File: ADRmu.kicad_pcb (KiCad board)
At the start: 4 copper layers, 160 x 100 mm, 67 parts, among them J1 DIN41612_02x16_AC_EvenPins, J10 Conn_01x01, J11 Conn_01x01, J12 Conn_01x01, J2 10Vf, J3 10Vs, J4 ADRf, J5 ADRs, J6 return, J7 guard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

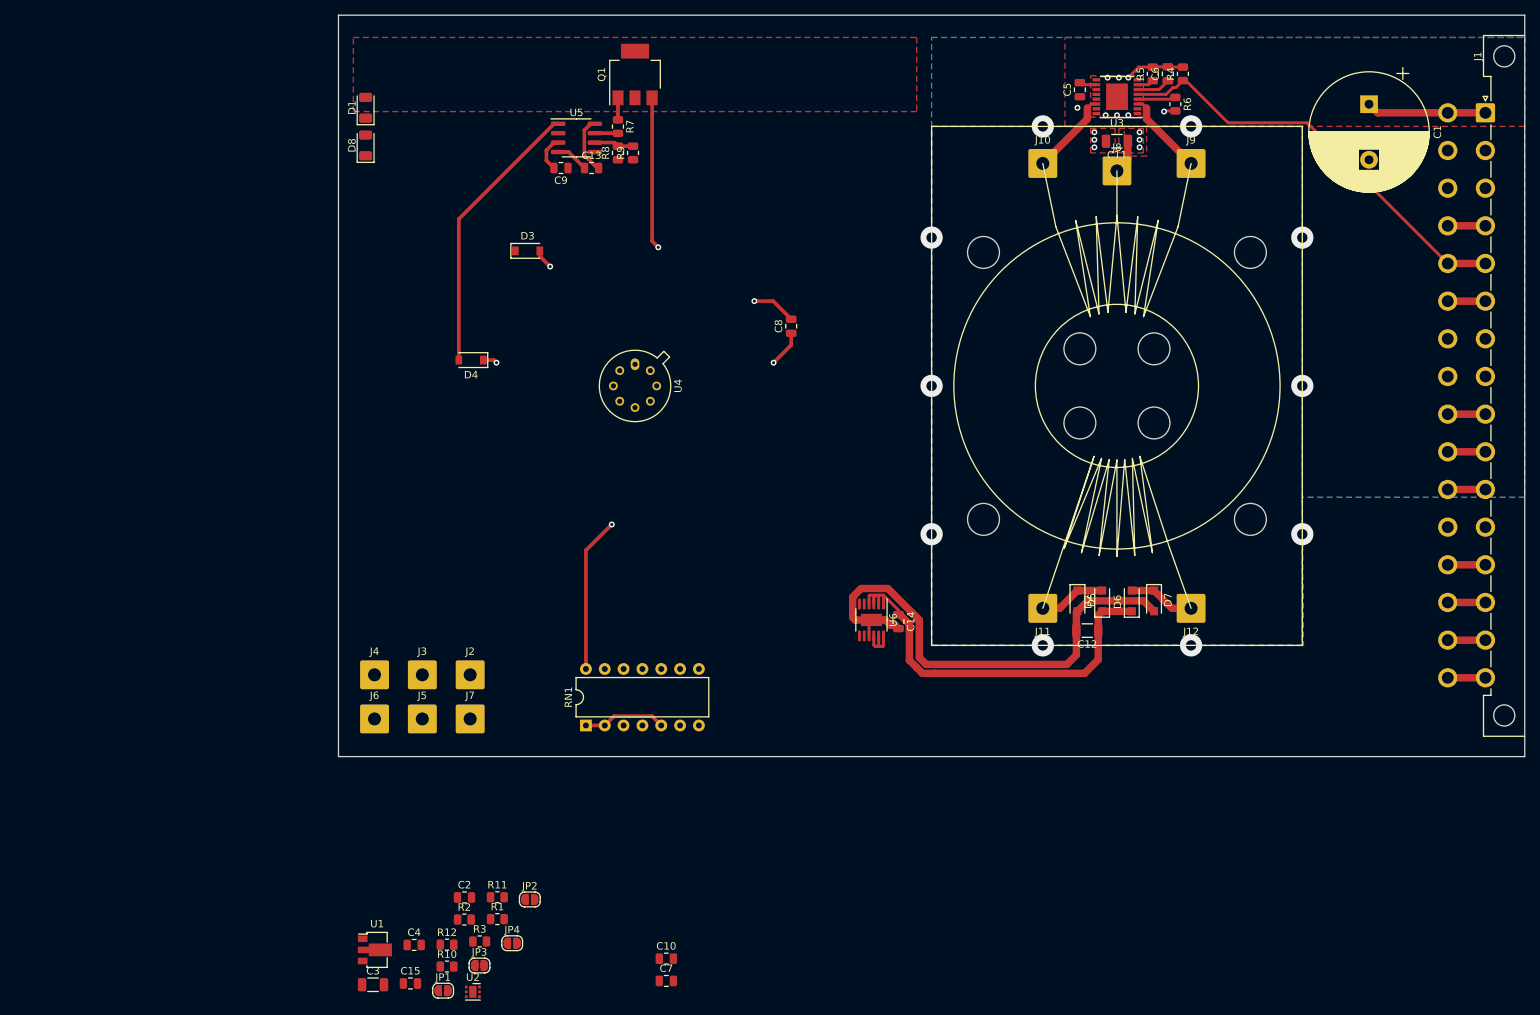
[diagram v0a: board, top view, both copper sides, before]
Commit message: added i2c temperature sensor and eeprom
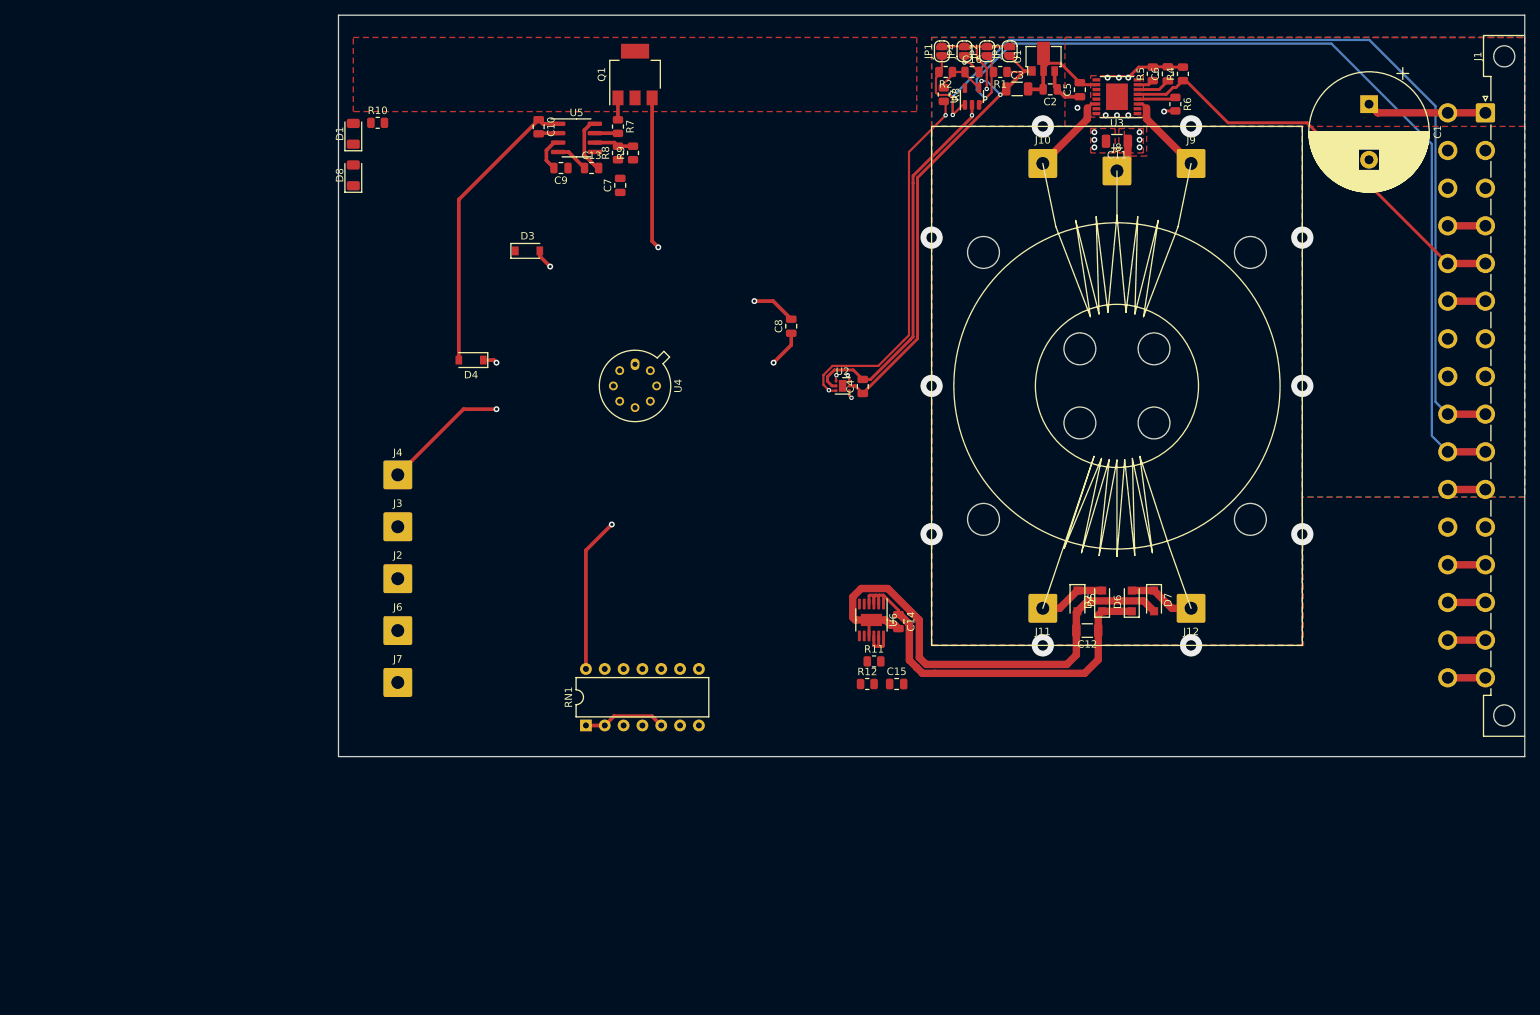
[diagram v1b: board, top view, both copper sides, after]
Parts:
- removed J5: ADRs, Connector_Wire:SolderWire-1sqmm_1x01_D1.4mm_OD3.9mm
- added C16: 100n, Capacitor_SMD:C_0805_2012Metric, F.Cu at (155.4, 57.7)
- added U7: 24AA02-OT, Package_TO_SOT_SMD:SOT-23-5, F.Cu at (155.4, 61.0)
- J4: value ADRf -> ADR
- moved U1 150.3 mm to (165.1, 55.9), turned to 90 degrees
- moved C3 148.8 mm to (161.5, 59.9)
- moved JP1 143.5 mm to (151.4, 54.9), turned to 90 degrees
- moved JP3 142.5 mm to (160.5, 54.9), turned to 90 degrees
- moved JP4 134.9 mm to (154.4, 54.9), turned to 90 degrees
- moved C2 134.6 mm to (166.0, 60.0), turned to 180 degrees
- moved R1 132.9 mm to (159.3, 57.7), turned to 180 degrees
- moved R2 131.5 mm to (151.9, 57.7), turned to 180 degrees
- moved R3 130.2 mm to (151.6, 60.7), turned to -90 degrees
- moved JP2 130.0 mm to (157.5, 54.9), turned to 90 degrees
- moved R10 114.2 mm to (75.3, 64.5)
- moved C10 113.5 mm to (97.0, 65.0), turned to -90 degrees
- moved C7 107.5 mm to (108.0, 73.0), turned to 90 degrees
- moved C4 96.6 mm to (140.7, 100.1), turned to 90 degrees
- moved U2 95.7 mm to (138.0, 100.0)
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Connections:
- J4 pad 1: /ref/ADRforce -> /ref/ADR_Pin3
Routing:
- net /DC-DC/SCL: track 5.08 -> 178.6 mm, vias 0 -> 2
- net /DC-DC/SDA: track 5.08 -> 175.3 mm, vias 0 -> 2
- net +3V3: track 0.00 -> 73.7 mm, vias 0 -> 2
- net Net-(JP1-Pad2): track 0.00 -> 66.1 mm, vias 0 -> 2
- net GND: track 22.4 -> 88.4 mm, vias 10 -> 12
- net Net-(R3-Pad2): track 0.00 -> 50.8 mm, vias 0 -> 2
- net /ref/ADR_Pin3: track 45.3 -> 62.3 mm, vias 1 -> 2
- net +12V: track 20.8 -> 26.9 mm
- net /ref/ADR_Pin4: track 33.7 -> 36.4 mm
- net Net-(C10-Pad1): track 37.8 -> 39.7 mm

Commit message: asas
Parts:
- added C17: 22u, Capacitor_SMD:C_1206_3216Metric, F.Cu at (122.7, 161.3)
- added Q2: MMBT3904, Package_TO_SOT_SMD:SOT-23, F.Cu at (122.3, 165.2)
- added R13: dnp, Resistor_SMD:R_0805_2012Metric, F.Cu at (125.5, 141.2)
- added R14: dnp, Crystal:Crystal_HC52-U_Vertical, F.Cu at (125.5, 143.1)
- added R15: 0, Resistor_SMD:R_0805_2012Metric, F.Cu at (107.1, 161.1)
- added R16: 0, Crystal:Crystal_HC52-U_Vertical, F.Cu at (98.0, 167.5)
- added R17: 0, Resistor_SMD:R_0805_2012Metric, F.Cu at (107.1, 164.0)
- added R18: 0, Crystal:Crystal_HC52-U_Vertical, F.Cu at (98.0, 162.2)
- added R19: 5k, Resistor_SMD:R_0805_2012Metric, F.Cu at (127.0, 164.4)
- added R20: 200k, Resistor_SMD:R_0805_2012Metric, F.Cu at (132.1, 161.1)
- added R21: 1.8M, Resistor_SMD:R_0805_2012Metric, F.Cu at (131.4, 164.0)
- added R22: 49.9k, Resistor_SMD:R_0805_2012Metric, F.Cu at (127.7, 161.1)
- moved JP1 1.02 mm to (151.4, 55.9)
- moved JP2 1.02 mm to (157.5, 55.9)
- moved JP3 1.02 mm to (160.5, 55.9)
- moved JP4 1.02 mm to (154.4, 55.9)
- moved C16 1.02 mm to (155.4, 58.7)
- moved C2 1.02 mm to (166.0, 61.0)
- moved C3 1.02 mm to (161.5, 61.0)
- moved R1 1.02 mm to (159.3, 58.7)
- moved R2 1.02 mm to (151.9, 58.7)
- moved R3 1.02 mm to (151.6, 61.7)
- moved U1 1.02 mm to (165.1, 56.9)
- moved U7 1.02 mm to (155.4, 62.0)
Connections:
- C12 pad 2: Net-(C14-Pad2) -> /ref/GNDf
- C14 pad 2: Net-(C14-Pad2) -> /ref/GNDf
- C15 pad 2: Net-(C14-Pad2) -> /ref/GNDf
- D5 pad 2: Net-(C14-Pad2) -> /ref/GNDf
- D7 pad 2: Net-(C14-Pad2) -> /ref/GNDf
- D8 pad 1: unconnected-(D8-Pad1) -> /ref/GNDf
- D8 pad 2: unconnected-(D8-Pad2) -> Net-(D8-Pad2)
- J1 pad a14: unconnected-(J1-Pada14) -> /DC-DC/status
- J1 pad a16: unconnected-(J1-Pada16) -> GND
- J1 pad c14: unconnected-(J1-Padc14) -> /DC-DC/status
- J1 pad c16: unconnected-(J1-Padc16) -> GND
- R11 pad 2: Net-(C14-Pad2) -> /ref/GNDf
- R12 pad 2: Net-(C14-Pad2) -> /ref/GNDf
- RN1 pad 12: /ref/ADR_Pin7 -> Net-(RN1-Pad12)
- RN1 pad 4: /ref/ADR_Pin7 -> Net-(RN1-Pad4)
- U6 pad 10: Net-(U6-Pad10) -> /ref/12Vf
- U6 pad 11: Net-(U6-Pad10) -> /ref/12Vf
- U6 pad 12: Net-(U6-Pad10) -> /ref/12Vf
- U6 pad 13: Net-(C14-Pad2) -> /ref/GNDf
- U6 pad 5: unconnected-(U6-Pad5) -> /DC-DC/PG
- U6 pad 7: unconnected-(U6-Pad7) -> Net-(U6-Pad7)
- U6 pad 9: Net-(C14-Pad2) -> /ref/GNDf
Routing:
- net Net-(C14-Pad2): track 67.7 -> 0.00 mm
- net /ref/GNDf: track 0.00 -> 67.7 mm
- net GND: track 88.4 -> 77.2 mm
- net Net-(U6-Pad10): track 5.37 -> 0.00 mm
- net /ref/12Vf: track 0.00 -> 5.37 mm
- net /DC-DC/SCL: track 178.6 -> 174.2 mm, vias 2 -> 3
- net +12V: track 26.9 -> 29.4 mm
- net Net-(JP1-Pad2): track 66.1 -> 64.7 mm
- net Net-(R3-Pad2): track 50.8 -> 49.6 mm, vias 2 -> 1
- net +3V3: track 73.7 -> 72.7 mm

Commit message: asdf
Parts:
- moved R21 38.9 mm to (146.6, 128.3), turned to -90 degrees
- moved C17 35.5 mm to (139.4, 130.0), turned to 90 degrees
- moved Q2 35.3 mm to (127.5, 130.3)
- moved R22 34.9 mm to (146.6, 131.8), turned to -90 degrees
- moved R20 25.5 mm to (142.7, 137.9), turned to 180 degrees
- moved R12 14.2 mm to (143.7, 126.2), turned to 180 degrees
- moved C15 11.9 mm to (143.7, 128.5), turned to 180 degrees
- moved R19 7.43 mm to (129.5, 157.5)
- moved C14 6.82 mm to (139.7, 135.3), turned to 90 degrees
- moved R11 4.70 mm to (146.6, 135.3), turned to 90 degrees
- moved U6 2.31 mm to (143.1, 133.5), turned to 90 degrees
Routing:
- net /ref/GNDf: track 67.7 -> 14.2 mm, vias 0 -> 11
- net Net-(C12-Pad1): track 54.9 -> 43.0 mm
- net Net-(C15-Pad1): track 0.00 -> 5.45 mm
- net /ref/12Vf: track 5.37 -> 0.00 mm
- net Net-(U6-Pad7): track 0.00 -> 4.93 mm
- net GND: track 77.2 -> 80.1 mm, vias 12 -> 15
- net Net-(R11-Pad1): track 0.00 -> 2.80 mm
- net /DC-DC/PG: track 0.00 -> 2.34 mm
- net Net-(JP1-Pad2): track 64.7 -> 65.4 mm
- net +3V3: track 72.7 -> 73.3 mm
- net Net-(R3-Pad2): track 49.6 -> 50.2 mm
- added copper zone on B.Cu, net /ref/GNDf
- added copper zone on F.Cu, net /ref/GNDf
- added copper zone on In1.Cu, net /ref/GNDf
- added copper zone on In2.Cu, net /ref/GNDf
- added copper zone on F.Cu, net Net-(C12-Pad1)

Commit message: asdf
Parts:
- moved R10 140.6 mm to (215.6, 56.1), turned to 135 degrees
- moved R19 92.9 mm to (215.1, 121.4)
- moved Q2 48.2 mm to (175.0, 138.4), turned to 90 degrees
- moved R6 2.09 mm to (180.8, 62.5)
- moved C5 0.11 mm to (170.0, 59.9)
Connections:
- C12 pad 2: /ref/GNDf -> /DC-DC/0Vout
- C13 pad 1: Net-(C13-Pad1) -> /DC-DC/0Vout
- C13 pad 2: Net-(C13-Pad2) -> /DC-DC/12Vout
- C14 pad 2: /ref/GNDf -> /DC-DC/0Vout
- C15 pad 2: /ref/GNDf -> /DC-DC/0Vout
- C17 pad 1: /ref/12Vf -> /DC-DC/12Vout
- C17 pad 2: /ref/GNDf -> /DC-DC/0Vout
- D3 pad 1: /ref/GNDf -> /DC-DC/0Vout
- D5 pad 2: /ref/GNDf -> /DC-DC/0Vout
- D7 pad 2: /ref/GNDf -> /DC-DC/0Vout
- D8 pad 1: /ref/GNDf -> /DC-DC/0Vout
- Q1 pad 2: /ref/12Vf -> /DC-DC/12Vout
- R11 pad 2: /ref/GNDf -> /DC-DC/0Vout
- R12 pad 2: /ref/GNDf -> /DC-DC/0Vout
- R21 pad 1: /ref/12Vf -> /DC-DC/12Vout
- R22 pad 2: /ref/GNDf -> /DC-DC/0Vout
- U5 pad 4: Net-(C13-Pad1) -> /DC-DC/0Vout
- U5 pad 8: Net-(C13-Pad2) -> /DC-DC/12Vout
- U6 pad 10: /ref/12Vf -> /DC-DC/12Vout
- U6 pad 11: /ref/12Vf -> /DC-DC/12Vout
- U6 pad 12: /ref/12Vf -> /DC-DC/12Vout
- U6 pad 13: /ref/GNDf -> /DC-DC/0Vout
- U6 pad 9: /ref/GNDf -> /DC-DC/0Vout
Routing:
- net Net-(D8-Pad2): track 0.00 -> 228.5 mm, vias 0 -> 2
- net GND: track 80.1 -> 245.2 mm, vias 15 -> 16
- net Net-(D1-Pad2): track 0.00 -> 149.2 mm, vias 0 -> 2
- net /DC-DC/status: track 0.00 -> 85.0 mm
- net /DC-DC/PG: track 2.34 -> 33.4 mm, vias 0 -> 2
- net /DC-DC/12Vout: track 0.00 -> 25.2 mm
- net /DC-DC/0Vout: track 0.00 -> 18.7 mm, vias 0 -> 11
- net /ref/GNDf: track 14.2 -> 0.00 mm, vias 11 -> 0
- net Net-(C13-Pad2): track 7.79 -> 0.00 mm
- net Net-(C13-Pad1): track 4.45 -> 0.00 mm
- net Net-(C12-Pad1): track 43.0 -> 45.9 mm
- net Net-(R6-Pad1): track 5.20 -> 3.18 mm
- added copper zone on B.Cu, net /DC-DC/0Vout
- added copper zone on F.Cu, net /DC-DC/0Vout
- added copper zone on In1.Cu, net /DC-DC/0Vout
- added copper zone on In2.Cu, net /DC-DC/0Vout
- added copper zone on F.Cu, net /DC-DC/12Vout
- removed copper zone on F.Cu, net /ref/12Vf
- removed copper zone on B.Cu, net /ref/GNDf
- removed copper zone on F.Cu, net /ref/GNDf
- removed copper zone on In1.Cu, net /ref/GNDf
- removed copper zone on In2.Cu, net /ref/GNDf

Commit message: started proto area
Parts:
- added NT1: NetTie_2, NetTie:NetTie-2_SMD_Pad0.5mm, F.Cu at (134.1, 142.2)
- added R23: dnp, Resistor_SMD:R_0805_2012Metric, F.Cu at (88.9, 141.6)
- added R24: dnp, Crystal:Crystal_HC52-U_Vertical, F.Cu at (88.9, 139.7)
- added R25: dnp, Resistor_SMD:R_0805_2012Metric, F.Cu at (73.7, 120.0)
- added R26: dnp, Crystal:Crystal_HC52-U_Vertical, F.Cu at (73.7, 118.1)
- added R27: dnp, Resistor_SMD:R_0805_2012Metric, F.Cu at (78.7, 120.0)
- added R28: dnp, Crystal:Crystal_HC52-U_Vertical, F.Cu at (78.7, 118.1)
- added R29: dnp, Resistor_SMD:R_0805_2012Metric, F.Cu at (78.7, 141.6)
- added R30: dnp, Crystal:Crystal_HC52-U_Vertical, F.Cu at (78.7, 143.5)
- added R31: dnp, Resistor_SMD:R_0805_2012Metric, F.Cu at (99.1, 141.6)
- added R32: dnp, Crystal:Crystal_HC52-U_Vertical, F.Cu at (99.1, 143.5)
- J6: value return -> LoSense
- J7: value guard -> GND
- moved R17 49.8 mm to (83.8, 120.0), turned to -90 degrees
- moved J2 49.6 mm to (35.6, 100.3)
- moved J3 49.6 mm to (35.6, 93.3)
- moved J4 49.6 mm to (35.6, 86.3)
- moved J6 49.6 mm to (35.6, 107.3)
- moved J7 49.6 mm to (35.6, 114.3)
- moved R18 46.3 mm to (83.8, 118.1), turned to -90 degrees
- moved R14 31.7 mm to (94.0, 139.7), turned to -90 degrees
- moved R13 31.5 mm to (94.0, 141.6), turned to -90 degrees
- moved R15 30.4 mm to (83.8, 141.6), turned to 90 degrees
- moved R16 27.9 mm to (83.8, 143.5), turned to 90 degrees
- moved RN1 27.1 mm to (78.7, 134.6)
- moved R19 2.41 mm to (215.1, 119.0)
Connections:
- D4 pad 1: /ref/ADR_Pin3 -> /ref/ADR
- J1 pad a26: /ref/guard -> /DC-DC/0Vout
- J1 pad a28: /ref/return -> Net-(J1-Pada28)
- J1 pad c26: /ref/guard -> /DC-DC/0Vout
- J1 pad c28: /ref/return -> Net-(J1-Pada28)
- J4 pad 1: /ref/ADR_Pin3 -> /ref/ADR
- J6 pad 1: /ref/return -> /DC-DC/0Vout
- J7 pad 1: /ref/guard -> /DC-DC/0Vout
- RN1 pad 1: /ref/ADR_Pin3 -> /ref/ADR
- RN1 pad 13: /ref/ADR_Pin8 -> Net-(RN1-Pad13)
- RN1 pad 14: /ref/ADR_Pin5 -> Net-(RN1-Pad14)
- RN1 pad 2: /ref/ADR_Pin3 -> /ref/ADR
- RN1 pad 5: /ref/ADR_Pin3 -> Net-(RN1-Pad5)
- RN1 pad 6: unconnected-(RN1-Pad6) -> Net-(R13-Pad1)
- RN1 pad 7: unconnected-(RN1-Pad7) -> Net-(RN1-Pad7)
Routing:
- net Net-(J1-Pada28): track 0.00 -> 92.9 mm
- net /ref/10Vsense: track 5.08 -> 91.4 mm
- net /ref/10Vforce: track 5.08 -> 89.9 mm
- net /ref/ADR: track 0.00 -> 62.3 mm, vias 0 -> 5
- net /ref/ADR_Pin3: track 62.3 -> 2.27 mm, vias 2 -> 1
- net /ref/ADR_Pin7: track 37.1 -> 69.6 mm, vias 1 -> 3
- net Net-(RN1-Pad13): track 0.00 -> 31.5 mm, vias 0 -> 11
- net /ref/ADR_Pin5: track 57.9 -> 41.8 mm, vias 1 -> 2
- net Net-(RN1-Pad7): track 0.00 -> 12.6 mm, vias 0 -> 3
- net Net-(RN1-Pad4): track 0.00 -> 9.66 mm, vias 0 -> 2
- net Net-(R13-Pad1): track 0.00 -> 9.66 mm, vias 0 -> 2
- net Net-(RN1-Pad5): track 0.00 -> 8.61 mm, vias 0 -> 2
- net Net-(RN1-Pad12): track 0.00 -> 7.62 mm, vias 0 -> 3
- net /ref/ADR_Pin6: track 33.7 -> 41.4 mm, vias 0 -> 3
- net Net-(RN1-Pad14): track 0.00 -> 6.07 mm, vias 0 -> 2
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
